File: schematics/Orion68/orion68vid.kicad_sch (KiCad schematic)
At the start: 25 parts, among them J300 Euro96pin, Q4 2N7000, U301 74HC245, U302 74HC245, U303 24LC256, U304 GAL16V8

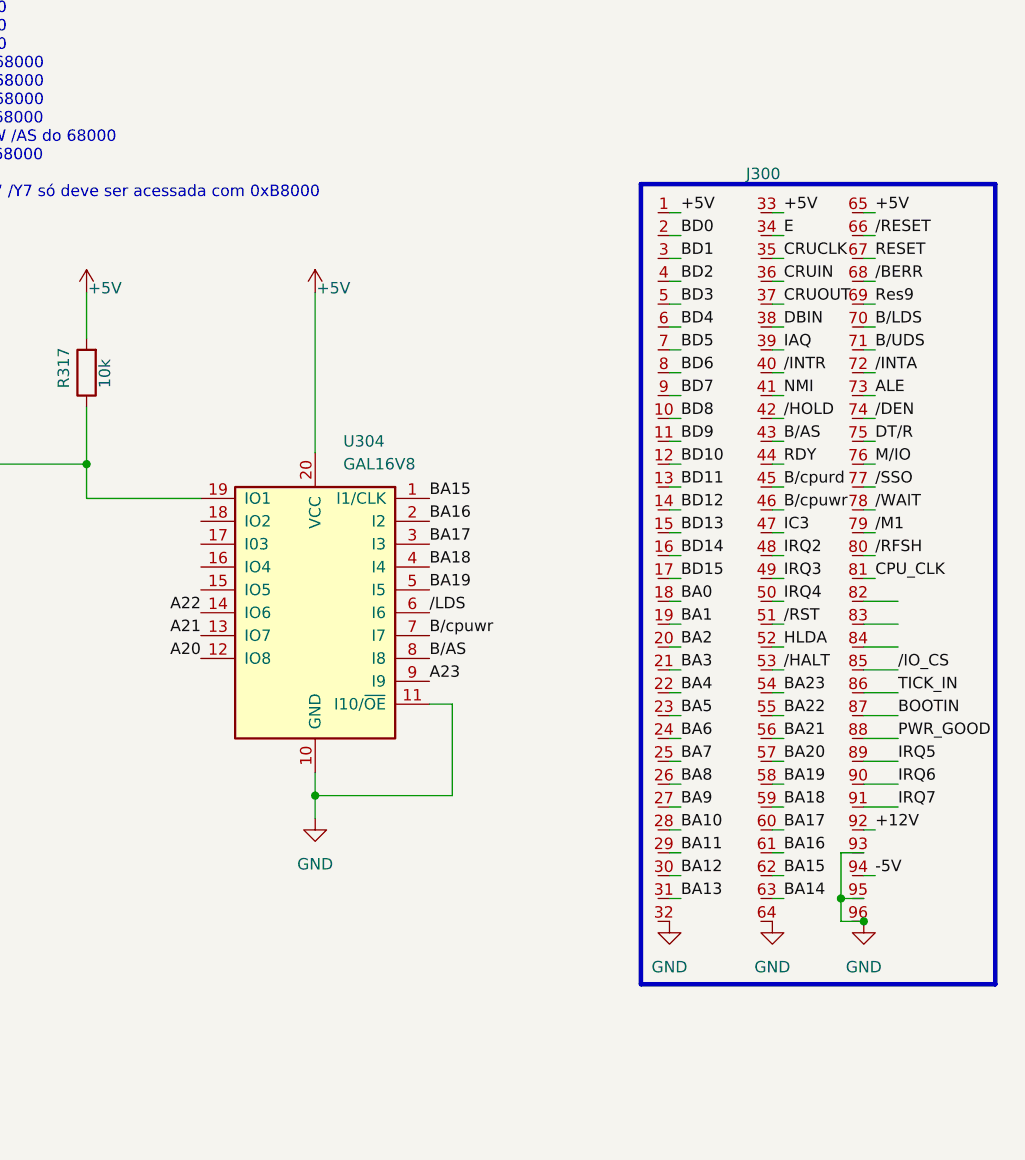
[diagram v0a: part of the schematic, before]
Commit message: B column DIN conn. all in GND
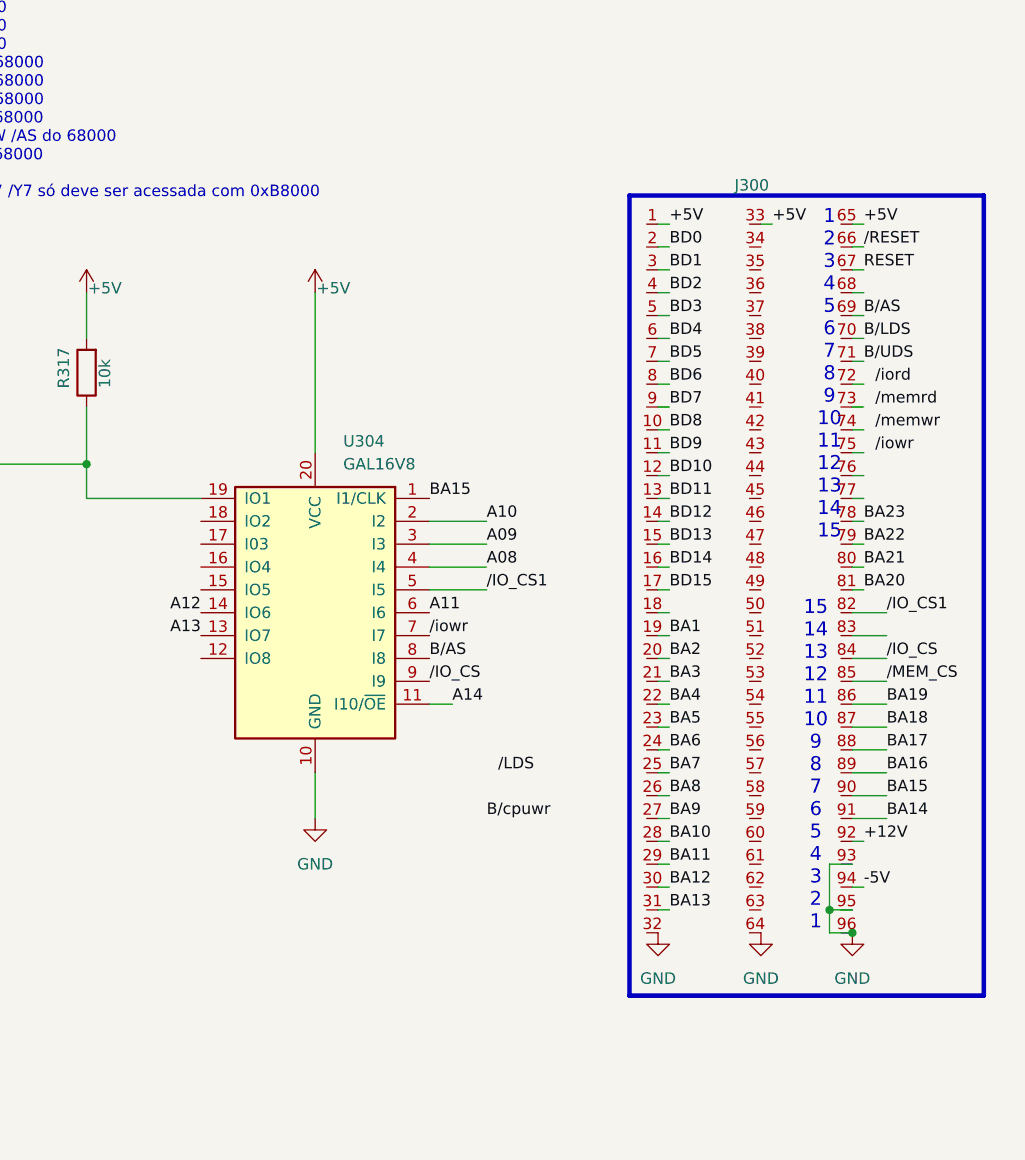
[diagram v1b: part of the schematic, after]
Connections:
- net A23 is gone; now on net /IO_CS: U304.9 (I9)
- net BOOTIN is gone; now on net BA18: J300.87
- net CPU_CLK is gone; now on net BA20: J300.81
- net IRQ5 is gone; now on net BA16: J300.89
- net IRQ6 is gone; now on net BA15: J300.90
- net IRQ7 is gone; now on net BA14: J300.91
- net PWR_GOOD is gone; now on net BA17: J300.88
- net Res9 is gone; now on net B/AS: J300.69
- net TICK_IN is gone; now on net BA19: J300.86
- net /M1 is gone; now on net BA22: J300.79
- net /RFSH is gone; now on net BA21: J300.80
- net /WAIT is gone; now on net BA23: J300.78
- net BA14: no longer J300.63
- net BA15: no longer J300.62
- net BA16: no longer J300.61, U304.2 (I2)
- net BA17: no longer J300.60, U304.3 (I3)
- net BA18: no longer J300.59, U304.4 (I4)
- net BA19: no longer J300.58, U304.5 (I5)
- net BA20: no longer J300.57
- net BA21: no longer J300.56
- net BA22: no longer J300.55
- net BA23: no longer J300.54
- net B/AS: no longer J300.43
- net B/cpuwr: no longer J300.46, U304.7 (I7)
- net GND: no longer U304.11 (I10/~{OE})
- net /IO_CS: now also J300.84; no longer J300.85
- net /LDS: no longer U304.6 (I6)
- net /IO_CS1: now reaches J300.82
- net /IO_CS1: now also U304.5 (I5)
- net A20: no longer names the net of U304.12 (IO8)
- net A21 renamed A13
- net A22 renamed A12
- net ALE: no longer names the net of J300.73
- net BA0: no longer names the net of J300.18
- net B/cpurd: no longer names the net of J300.45
- net CRUCLK: no longer names the net of J300.35
- net CRUIN: no longer names the net of J300.36
- net CRUOUT: no longer names the net of J300.37
- net DBIN: no longer names the net of J300.38
- net DT/R: no longer names the net of J300.75
- net E: no longer names the net of J300.34
- net HLDA: no longer names the net of J300.52
- net IAQ: no longer names the net of J300.39
- net IC3: no longer names the net of J300.47
- net IRQ2: no longer names the net of J300.48
- net IRQ3: no longer names the net of J300.49
- net IRQ4: no longer names the net of J300.50
- net M/IO: no longer names the net of J300.76
- net NMI: no longer names the net of J300.41
- net RDY: no longer names the net of J300.44
- net /BERR: no longer names the net of J300.68
- net /DEN: no longer names the net of J300.74
- net /HALT: no longer names the net of J300.53
- net /HOLD: no longer names the net of J300.42
- net /INTA: no longer names the net of J300.72
- net /INTR: no longer names the net of J300.40
- net /RST: no longer names the net of J300.51
- net /SSO: no longer names the net of J300.77
- new net A08: U304.4 (I4)
- new net A09: U304.3 (I3)
- new net A10: U304.2 (I2)
- new net A11: U304.6 (I6)
- new net A14: U304.11 (I10/~{OE})
- new net /MEM_CS: J300.85
- new net /iowr: U304.7 (I7)
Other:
- note added: "1 2 3 4 5 6 7 8 9 10 11 12 13 14 15"
- note added: "15 14 13 12 11 10 9 8 7 6 5 4 3 2 1"

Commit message: Update vbug2.0
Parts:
- added R25: 1k, Resistor_THT:R_Axial_DIN0204_L3.6mm_D1.6mm_P5.08mm_Horizontal, symbol Device:R
- added U19: 74LS541, symbol 74xx:74LS541
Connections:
- net +5V: now also R25.2, U19.20 (VCC)
- net BD0: now also U19.18 (Y0)
- net BD1: now also U19.17 (Y1)
- net BD2: now also U19.16 (Y2)
- net BD3: now also U19.15 (Y3)
- net BD4: now also U19.14 (Y4)
- net BD5: now also U19.13 (Y5)
- net BD6: now also U19.12 (Y6)
- net BD7: now also U19.11 (Y7)
- net GND: now also U300.13 (GND), U300.18 (GND), U300.23 (GND), U300.28 (GND), U300.3 (GND), U300.33 (GND), U300.38 (GND), U300.8 (GND), U301.1 (A->B), U301.10 (GND), U301.19 (CE), U302.1 (A->B), U302.10 (GND), U302.11 (B7), U302.12 (B6), U302.13 (B5), U302.19 (CE), U302.7 (A5), U302.8 (A6), U302.9 (A7), U303.1 (A0), U303.2 (A1), U303.3 (A2), U303.4 (GND), U303.7 (WP), U19.10 (GND)
- net /ST_CS: now reaches U304.18 (IO2)
- net /ST_CS: now also U19.1 (G1), U19.19 (G2)
- net D0: now reaches U300.1 (GP0), U301.2 (A0)
- net D7: now reaches U300.10 (GP7), U301.9 (A7)
- net D1: now reaches U300.2 (GP1), U301.3 (A1)
- net ST0: now reaches U300.27 (GP21)
- net ST0: now also R25.1, U19.2 (A0)
- net ST1: now reaches U300.29 (GP22)
- net ST1: now also U19.3 (A1)
- net ST2: now reaches U300.31 (GP26)
- net ST2: now also U19.4 (A2)
- net ST3: now reaches U300.32 (GP27)
- net ST3: now also U19.5 (A3)
- net ST4: now reaches U300.34 (GP28)
- net ST4: now also U19.6 (A4)
- net D2: now reaches U300.4 (GP2), U301.4 (A2)
- net D3: now reaches U300.5 (GP3), U301.5 (A3)
- net D4: now reaches U300.6 (GP4), U301.6 (A4)
- net D5: now reaches U300.7 (GP5), U301.7 (A5)
- net D6: now reaches U300.9 (GP6), U301.8 (A6)
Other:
- moved on the sheet: J300, Q4, R300, R301, R302, R303, R304, R305, R306, R307, R308, R309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

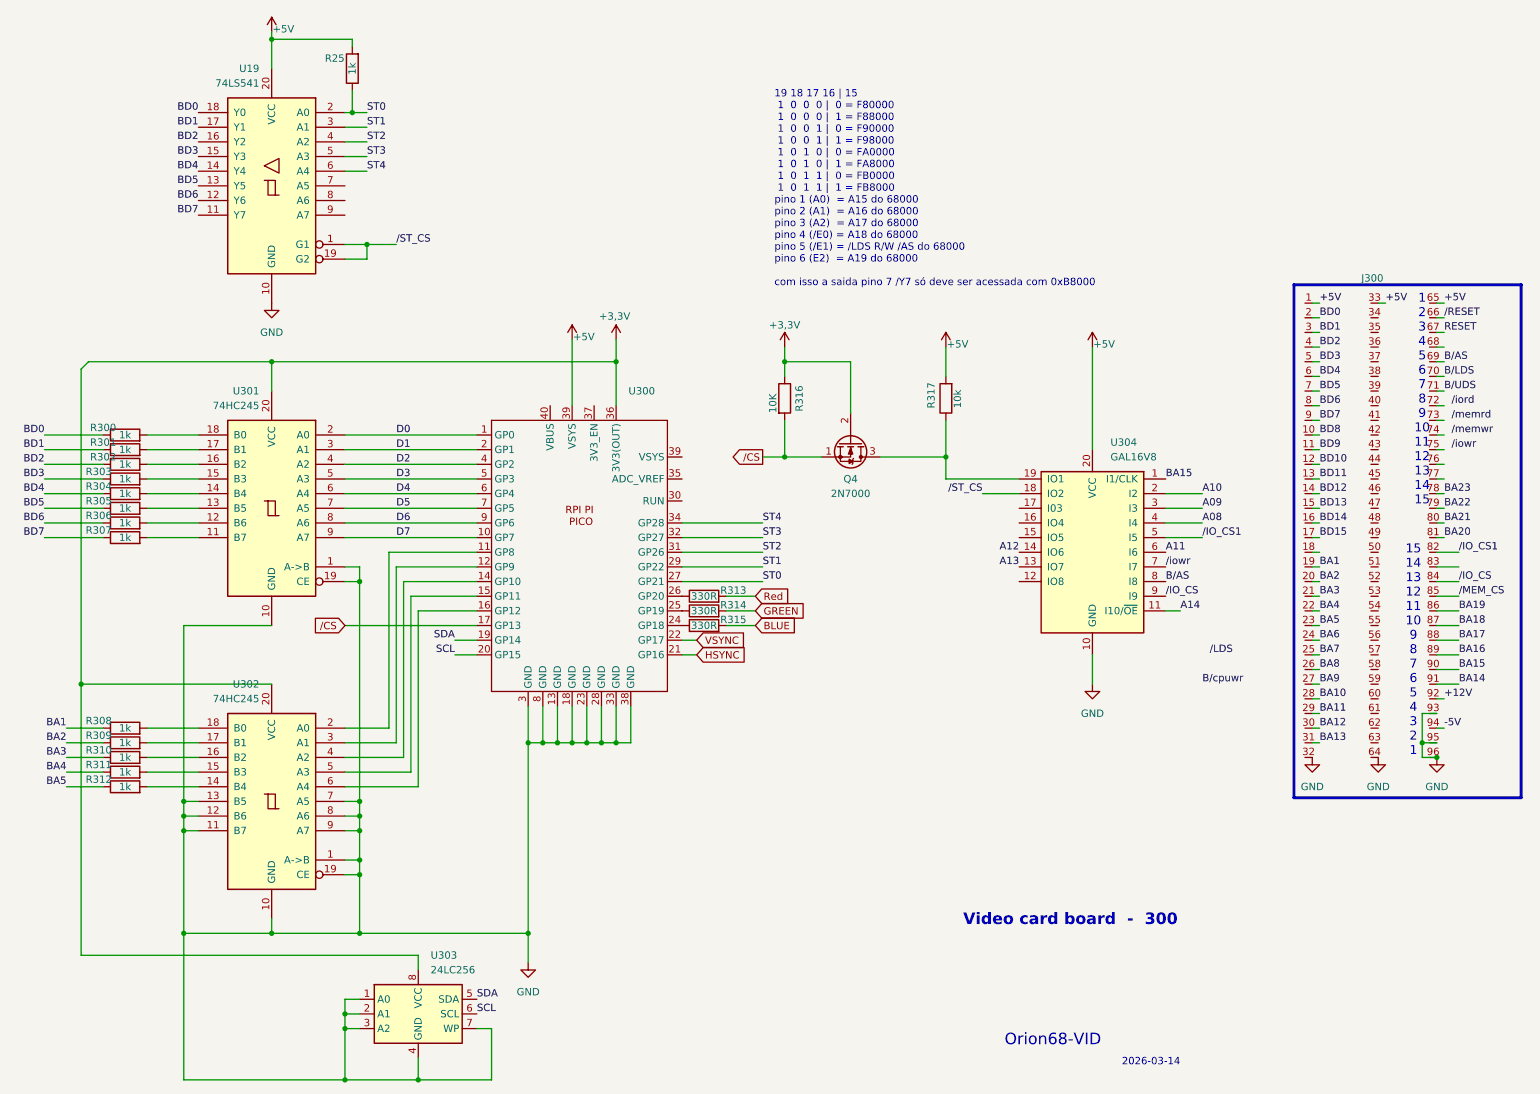
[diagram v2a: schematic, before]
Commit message: added card vga pico2,env68k,atmega8
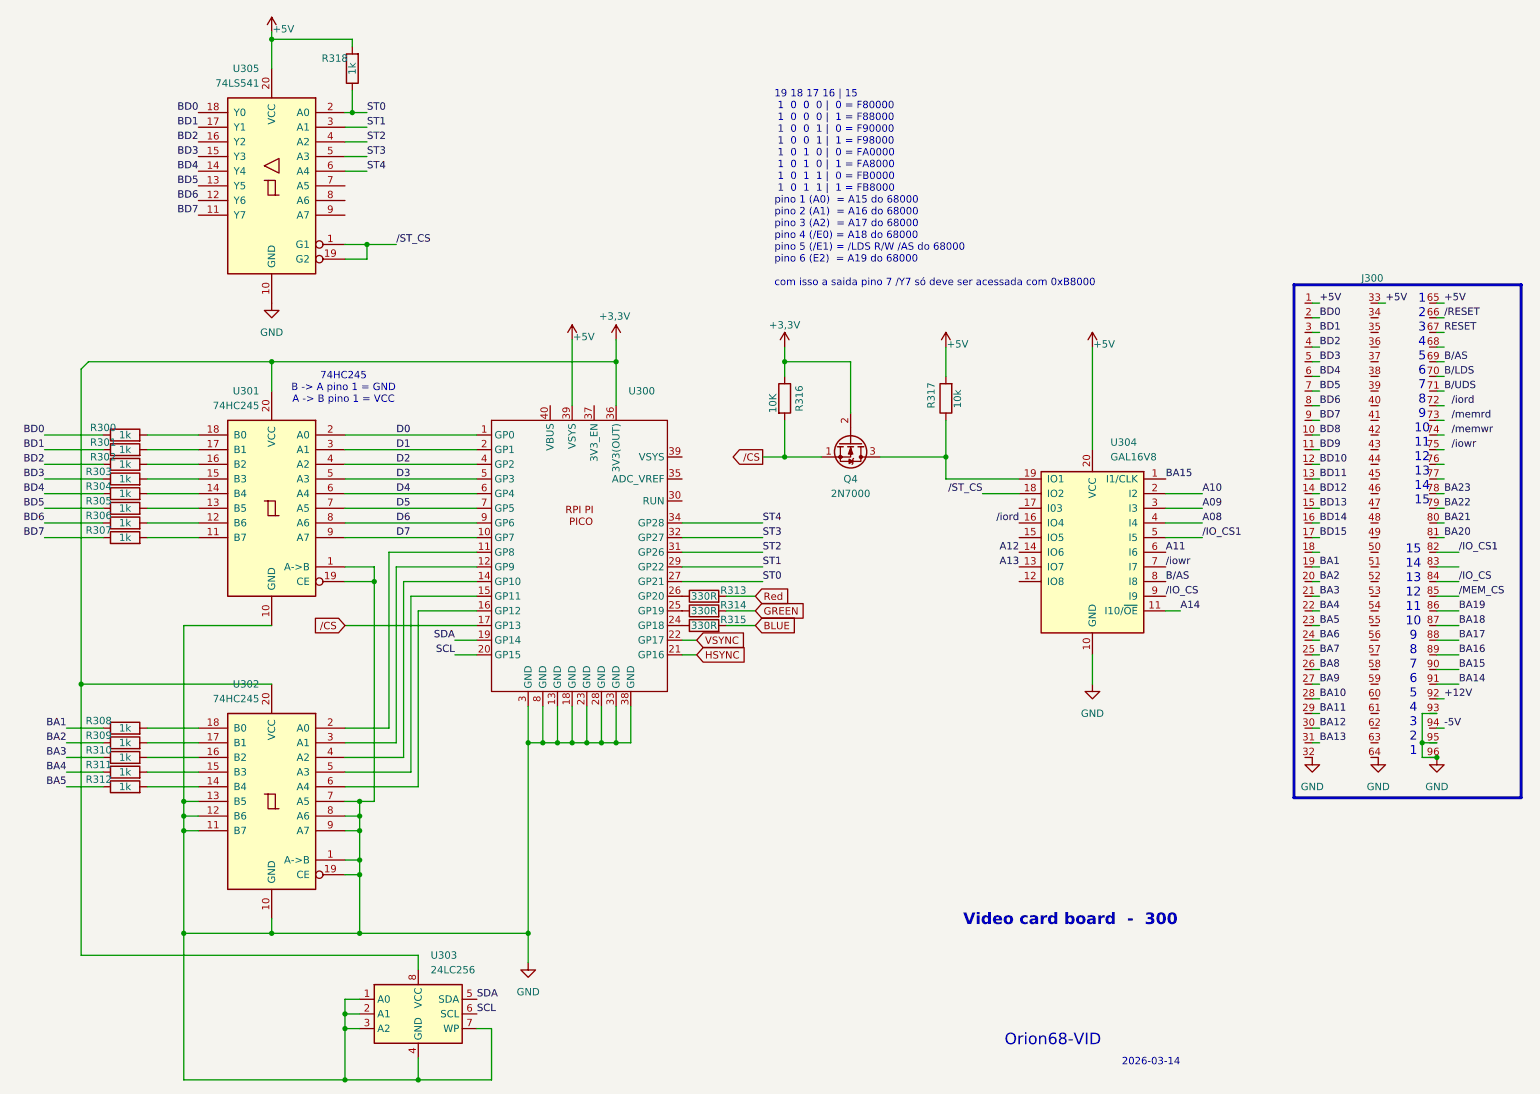
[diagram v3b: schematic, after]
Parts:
- renumbered R25 to R318, U19 to U305
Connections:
- net /iord: now also U304.16 (IO4)
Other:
- note added: "74HC245 B -> A pino 1 = GND A -> B pino 1 = VCC"

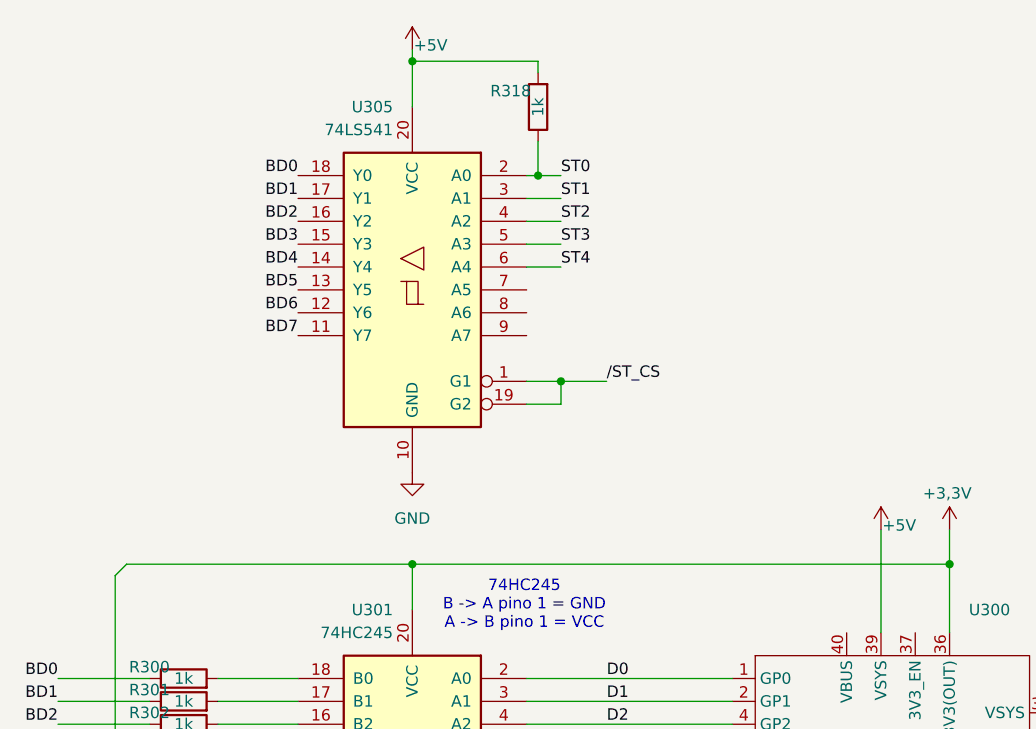
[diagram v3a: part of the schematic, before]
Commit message: New code for VBug2.0 with new reset system
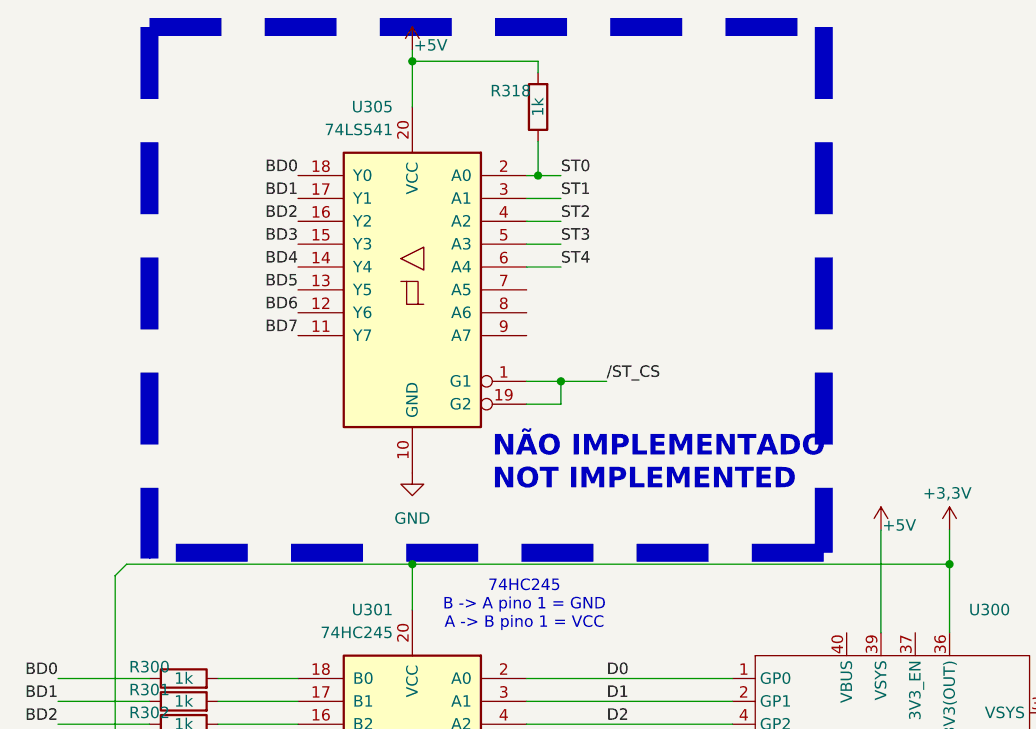
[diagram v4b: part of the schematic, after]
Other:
- note added: "NÃO IMPLEMENTADO NOT IMPLEMENTED"
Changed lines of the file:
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@@
+		)
+	)
+	(text "NÃO IMPLEMENTADO\nNOT IMPLEMENTED"
+		(exclude_from_sim no)
+		(at 69.85 61.214 0)
+		(effects
+			(font
+				(size 2.27 2.27)
+				(thickness 0.454)
+				(bold yes)
+				(color 255 0 0 1)
+			)
+			(justify left)
 		)
 	)
@@
 		)
 	)
+	(polyline
+		(pts
+			(xy 32.385 71.12) (xy 31.75 71.755)
+		)
+		(stroke
+			(width 0)
+			(type default)
+		)
+	)
 	(wire
 		(pts
@@
 		)
 	)
+	(polyline
+		(pts
+			(xy 106.68 12.7) (xy 106.68 71.12)
+		)
+		(stroke
+			(width 2)
+			(type dash)
+			(color 255 0 0 1)
+		)
+	)
 	(wire
 		(pts
@@
 		)
 	)
+	(polyline
+		(pts
+			(xy 31.75 12.7) (xy 106.68 12.7)
+		)
+		(stroke
+			(width 2)
+			(type dash)
+			(color 255 0 0 1)
+		)
+	)
 	(wire
 		(pts
@@
 		)
 	)
+	(polyline
+		(pts
+			(xy 106.68 71.12) (xy 32.385 71.12)
+		)
+		(stroke
+			(width 2)
+			(type dash)
+			(color 255 0 0 1)
+		)
+	)
 	(wire
 		(pts
@@
 		)
 	)
+	(polyline
+		(pts
+			(xy 31.75 12.7) (xy 31.75 71.755)
+		)
+		(stroke
+			(width 2)
+			(type dash)
+			(color 255 0 0 1)
+		)
+	)
